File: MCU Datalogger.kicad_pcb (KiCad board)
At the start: 2 copper layers, 29 parts, among them J1 Conn_01x04_Pin, J2 Conn_01x09_Pin, J3 Conn_01x04_Pin, J4 Conn_02x03_Odd_Even, U1 24LC1025, U2 24LC1025, U3 DS1337S_, U4 ATMEGA328P-AU, Y1 32.768 KHz, Y2 16 MHz

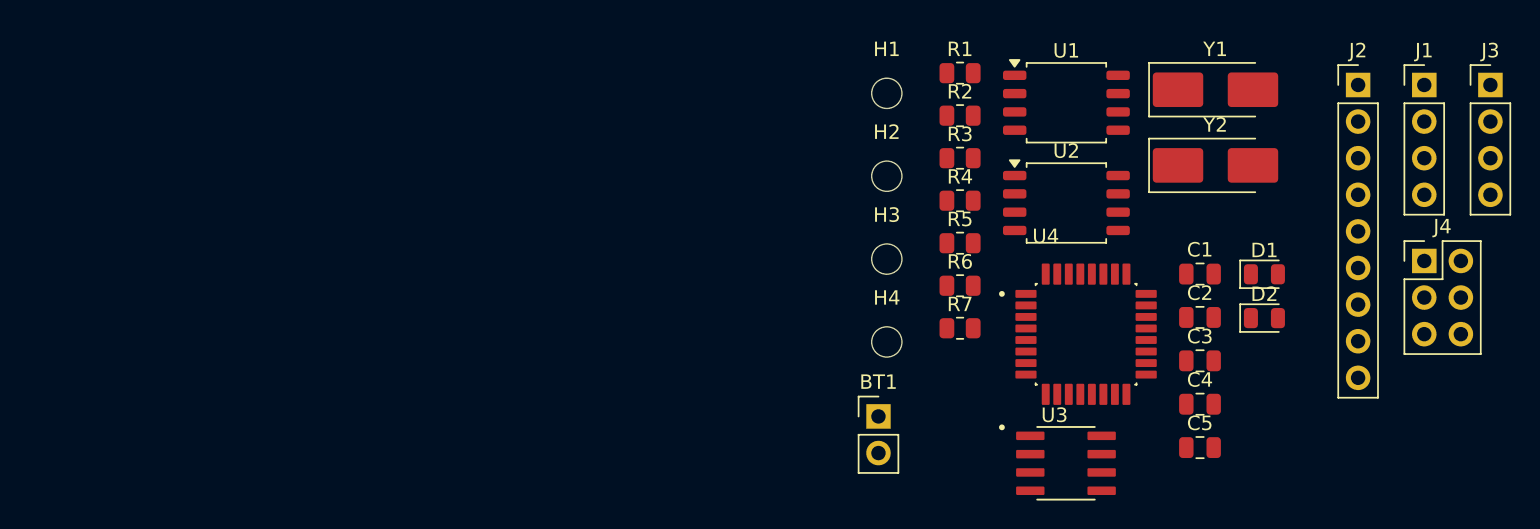
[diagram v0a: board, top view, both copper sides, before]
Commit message: finish 2 layer PCB Design
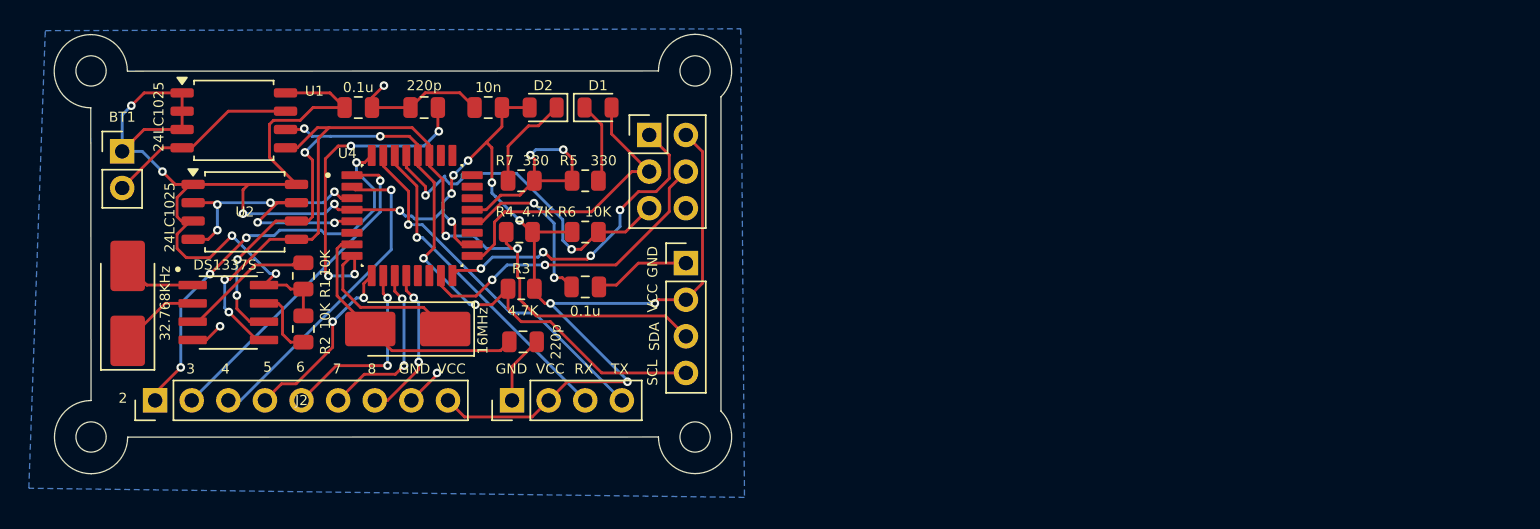
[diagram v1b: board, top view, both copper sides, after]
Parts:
- Y1: value 32.768 KHz -> 32.768KHz
- Y2: value 16 MHz -> 16MHz
- moved J2 86.3 mm to (71.8, 81.3), turned to 90 degrees
- moved Y1 76.9 mm to (69.8, 74.5), turned to 90 degrees
- moved J3 71.3 mm to (96.5, 81.3), turned to 90 degrees
- moved C1 59.5 mm to (85.9, 61.0)
- moved U3 59.1 mm to (76.8, 75.2)
- moved U1 57.8 mm to (77.2, 61.8)
- moved Y2 57.2 mm to (89.3, 76.3), turned to 180 degrees
- moved U2 57.0 mm to (78.0, 68.2)
- moved C3 56.6 mm to (90.4, 61.0), turned to 180 degrees
- moved H4 55.6 mm to (67.3, 83.8)
- moved BT1 55.6 mm to (69.5, 64.0)
- moved H1 55.2 mm to (67.3, 58.4)
- moved C5 54.7 mm to (94.9, 61.0), turned to 180 degrees
- moved J4 54.5 mm to (106.0, 62.9)
- moved J1 52.7 mm to (108.6, 71.8)
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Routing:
- net /Vcc: track 0.00 -> 156.1 mm, vias 0 -> 16
- net GND: track 0.00 -> 81.4 mm, vias 0 -> 11
- net /SDA: track 0.00 -> 62.2 mm, vias 0 -> 4
- net /SCL: track 0.00 -> 60.3 mm, vias 0 -> 7
- net Net-(U4-PB7): track 0.00 -> 32.6 mm, vias 0 -> 4
- net /D2: track 0.00 -> 28.9 mm, vias 0 -> 4
- net /TX: track 0.00 -> 25.4 mm, vias 0 -> 1
- net /RST: track 0.00 -> 24.4 mm, vias 0 -> 2
- net /D3: track 0.00 -> 22.9 mm, vias 0 -> 1
- net /RX: track 0.00 -> 22.7 mm, vias 0 -> 1
- net /D4: track 0.00 -> 22.6 mm, vias 0 -> 1
- net /MOSI: track 0.00 -> 22.5 mm, vias 0 -> 2
- net /MISO: track 0.00 -> 22.5 mm, vias 0 -> 4
- net /SCK: track 0.00 -> 21.1 mm
- net Net-(U4-PB6): track 0.00 -> 18.2 mm
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- added copper zone on B.Cu, net GND
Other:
- board outline added: 47 x 30.5 mm
- board text added: "2"
- board text added: "3"
- board text added: "4"
- board text added: "5"
- board text added: "6"
- board text added: "7"
- board text added: "8"
- board text added: "GND"
- board text added: "RX"
- board text added: "SCL"
- board text added: "SDA"
- board text added: "TX"
- board text added: "VCC"
